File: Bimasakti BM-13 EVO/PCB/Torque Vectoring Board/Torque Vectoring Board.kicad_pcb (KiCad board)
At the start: 2 copper layers, 108 x 104.9 mm, 32 parts, among them J1 SIGNAL 1, J2 SIGNAL 2, U3 SN65HVD230, U4 SN65HVD230, U5 ADS1115IDGS

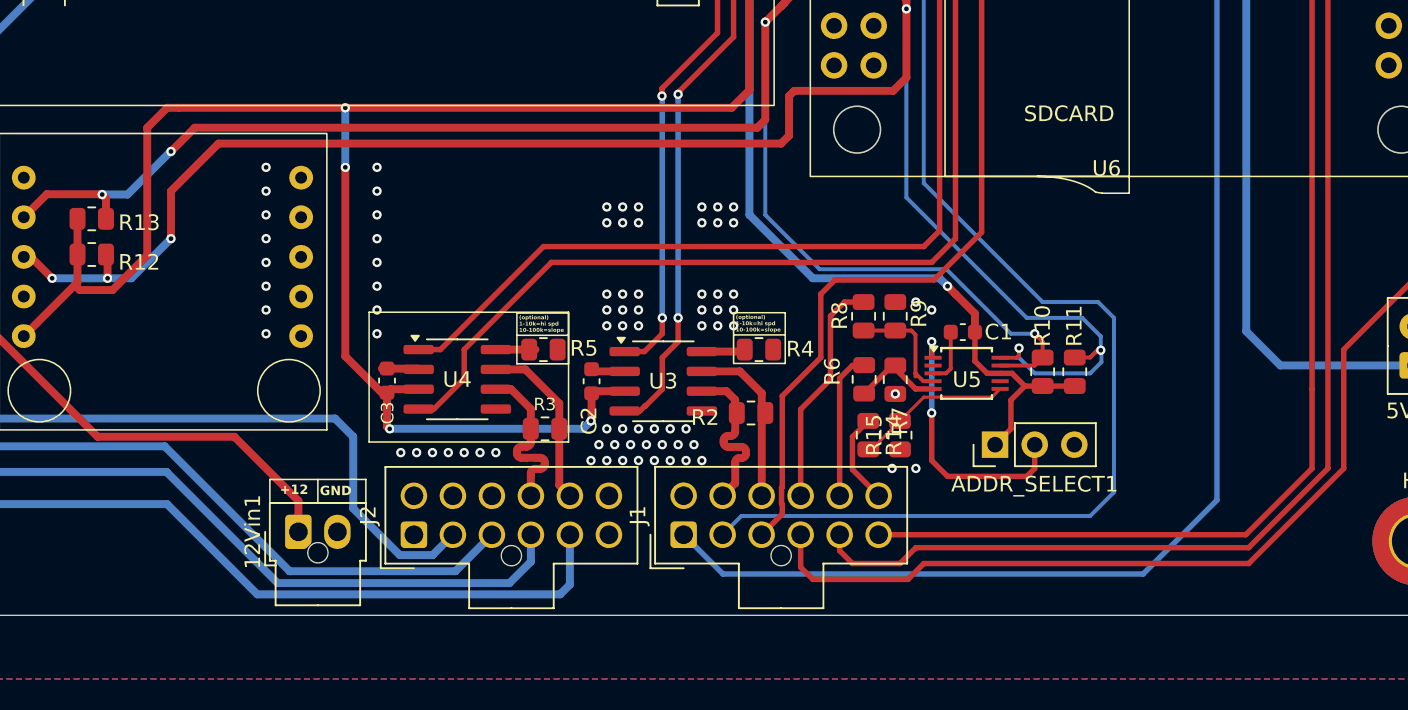
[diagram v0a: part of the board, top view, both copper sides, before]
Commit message: update footprint and pneumatic
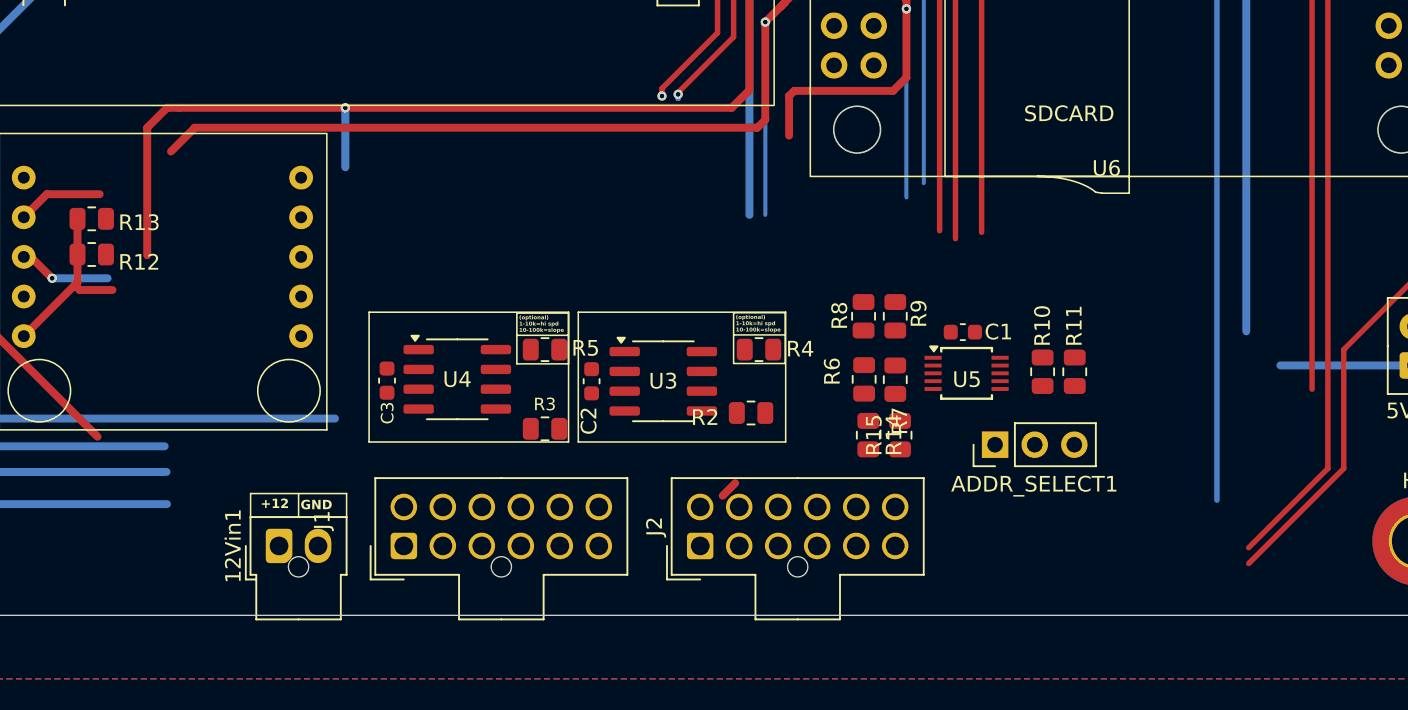
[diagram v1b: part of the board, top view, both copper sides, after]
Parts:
- moved J2 18.4 mm to (102.0, 134.0)
- moved J1 18.0 mm to (83.0, 134.0)
- moved 12Vin1 1.53 mm to (75.0, 134.0)
- moved R5 0.10 mm to (92.1, 121.4)
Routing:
- net SCL: track 115.5 -> 36.1 mm, vias 6 -> 2
- net 3V3: track 234.0 -> 161.6 mm, vias 7 -> 3
- net MISO: track 122.4 -> 69.3 mm
- net CAN2_RX: track 118.3 -> 78.3 mm
- net SCK: track 169.4 -> 132.2 mm
- net CAN2_TX: track 117.0 -> 80.5 mm
- net STM_RX: track 71.5 -> 36.8 mm
- net SDA: track 101.3 -> 68.5 mm, vias 4 -> 1
- net WS_FR: track 93.6 -> 61.9 mm
- net SS: track 165.7 -> 134.1 mm
- net MOSI: track 113.2 -> 84.2 mm
- net WS_FL: track 83.8 -> 55.2 mm
- net STM_TX: track 78.1 -> 50.1 mm
- net WS_RR: track 74.5 -> 49.3 mm
- net CAN1_RX: track 62.1 -> 40.0 mm, vias 2 -> 1
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
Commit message: update tv board
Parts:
- added J3: wsout1, TerminalBlock_Phoenix:TerminalBlock_Phoenix_PT-1,5-2-5.0-H_1x02_P5.00mm_Horizontal, F.Cu at (110.8, 42.9)
- added J4: wsout2, TerminalBlock_Phoenix:TerminalBlock_Phoenix_PT-1,5-2-5.0-H_1x02_P5.00mm_Horizontal, F.Cu at (122.5, 42.9)
- moved U1 90.8 mm to (83.3, 115.8), turned to 180 degrees
- moved U2 62.7 mm to (129.1, 139.6)
- moved R12 62.3 mm to (125.1, 120.9), turned to 180 degrees
- moved R13 62.3 mm to (125.1, 118.6), turned to 180 degrees
- moved U6 43.2 mm to (123.4, 36.2)
- moved R4 39.7 mm to (66.9, 113.4), turned to -90 degrees
- moved R2 36.1 mm to (69.3, 121.6)
- moved U3 29.1 mm to (71.7, 115.2), turned to 180 degrees
- moved ADDR_SELECT1 26.2 mm to (102.4, 109.0)
- moved R9 24.2 mm to (90.5, 122.7), turned to 0 degrees
- moved R8 22.6 mm to (90.5, 124.8), turned to 0 degrees
- moved C2 20.0 mm to (76.8, 115.3), turned to -90 degrees
- moved R3 19.7 mm to (109.0, 116.5), turned to -90 degrees
- moved C3 19.3 mm to (99.3, 115.0)
- moved R7 19.2 mm to (95.4, 122.7), turned to 0 degrees
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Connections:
- U1 pad 72: GPOS -> unconnected-(U1-PA6-Pad72)
- U6 pad 25: GND -> STM_RX
- U6 pad 26: GND -> unconnected-(U6-GND-Pad26)
- U6 pad 27: GND -> STM_TX
- U6 pad 29: GND -> SCL
- U6 pad 31: GND -> SDA
- U6 pad 4: GND -> WS_FRo
- U6 pad 5: GND -> WS_FLo
- U6 pad 6: GND -> WS_RRo
- U6 pad 7: GND -> WS_RLo
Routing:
- net STM_TX: track 50.1 -> 271.9 mm
- net STM_RX: track 36.8 -> 186.6 mm
- net SCL: track 36.1 -> 178.7 mm, vias 2 -> 0
- net SDA: track 68.5 -> 168.4 mm
- net SCK: track 132.2 -> 208.9 mm, vias 2 -> 0
- net SS: track 134.1 -> 204.4 mm
- net MISO: track 69.3 -> 137.9 mm
- net MOSI: track 84.2 -> 133.7 mm, vias 3 -> 0
- net 12V: track 79.1 -> 123.3 mm, vias 1 -> 0
- net WS_RLo: track 0.00 -> 43.0 mm
- net 3V3: track 161.6 -> 126.6 mm, vias 3 -> 1
- net 5V: track 156.8 -> 191.4 mm, vias 2 -> 1
- net ESC1_LO: track 0.00 -> 31.6 mm
- net WS_RRo: track 0.00 -> 31.4 mm
- net ESC1_HI: track 0.00 -> 30.7 mm
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
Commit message: tv dengan pdm kecil
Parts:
- added G***: LOGO, 0_logo:altium 12x12, F.Cu at (50.5, 117.5)
- added G***: LOGO, 0_logo:logo bimsak, F.Cu at (126.0, 111.0)
- added G***: LOGO, 0_logo:ugm 7.8x7.8, F.Cu at (134.5, 111.0)
- added a: LOGO, 0_logo:11jembo_tulisan_12x8.7, F.Cu at (51.0, 124.5)
- J3, J4: footprint TerminalBlock_Phoenix:TerminalBlock_Phoenix_PT-1,5-2-5.0-H_1x02_P5.00mm_Horizontal -> Connector_Molex:Molex_Nano-Fit_105309-xx02_1x02_P2.50mm_Vertical
- U6: footprint 0_CUSTOM_PCB:wheelspeed -> 0_WHEELSPEED:Untitled
- moved U6 25.6 mm to (114.3, 60.0)
- moved H4 10.2 mm to (138.0, 136.0)
- moved 5Vin1 9.99 mm to (138.3, 119.9)
- moved H2 9.95 mm to (138.0, 38.0)
- moved 12Vin1 9.88 mm to (65.3, 133.0)
- moved C1 9.88 mm to (102.1, 125.8)
- moved J1 9.88 mm to (73.3, 133.0)
- moved J2 9.88 mm to (92.3, 133.0)
- moved R10 9.88 mm to (103.8, 125.6)
- moved R12 9.88 mm to (115.4, 123.0)
- moved R13 9.88 mm to (115.4, 120.7)
- moved R4 9.88 mm to (57.2, 115.5)
- moved R5 9.88 mm to (99.8, 115.5)
- moved R8 9.88 mm to (80.9, 126.9)
- moved U5 9.88 mm to (97.9, 125.5)
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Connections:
- J1 pad 5: STM_TX -> STM_TX_2
- J1 pad 6: STM_RX -> STM_RX_2
- J2 pad 1: unconnected-(J2-Pin_1-Pad1) -> GND
- J2 pad 12: unconnected-(J2-Pin_12-Pad12) -> GND
- J2 pad 6: unconnected-(J2-Pin_6-Pad6) -> GND
- J2 pad 7: unconnected-(J2-Pin_7-Pad7) -> GND
- J2 pad 8: unconnected-(J2-Pin_8-Pad8) -> GND
- J2 pad 9: unconnected-(J2-Pin_9-Pad9) -> GND
- U1 pad 28: unconnected-(U1-PC12-Pad28) -> STM_TX_2
- U1 pad 29: unconnected-(U1-PD2-Pad29) -> STM_RX_2
- U6 pad 10: GND -> WS_RRo
- U6 pad 11: GND -> WS_FLo
- U6 pad 12: GND -> WS_FRo
- U6 pad 13: GND -> SDA
- U6 pad 14: GND -> SCL
- U6 pad 3: GND -> STM_TX
- U6 pad 4: WS_FRo -> STM_RX
- U6 pad 5: WS_FLo -> WS_RR
- U6 pad 6: WS_RRo -> WS_RL
- U6 pad 7: WS_RLo -> WS_FR
- U6 pad 8: GND -> WS_FL
- U6 pad 9: GND -> WS_RLo
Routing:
- net STM_TX: track 271.9 -> 110.9 mm, vias 0 -> 2
- net SCK: track 208.9 -> 91.7 mm
- net SS: track 204.4 -> 104.2 mm, vias 1 -> 0
- net STM_RX_2: track 0.00 -> 84.7 mm, vias 0 -> 1
- net STM_RX: track 186.6 -> 102.3 mm, vias 1 -> 2
- net 12V: track 123.3 -> 205.2 mm
- net SCL: track 178.7 -> 101.4 mm, vias 0 -> 1
- net STM_TX_2: track 0.00 -> 73.1 mm
- net SDA: track 168.4 -> 106.2 mm, vias 1 -> 0
- net WS_FRo: track 17.2 -> 65.0 mm
- net MOSI: track 133.7 -> 86.9 mm
- net MISO: track 137.9 -> 91.9 mm
- net WS_FLo: track 21.8 -> 58.6 mm
- net WS_RL: track 44.3 -> 78.8 mm
- net WS_RR: track 51.7 -> 77.8 mm, vias 0 -> 1
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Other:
- board size 108 x 104.9 mm -> 99 x 108 mm
- board text added: "5V"
- board text added: "APPS IN_1"
- board text added: "APPS IN_2"
- board text added: "ESC1 HI"
- board text added: "ESC1 LO"
- board text added: "ESC2 HI"
- board text added: "ESC2 LO"
- board text added: "MISO"
- board text added: "MOSI"
- board text added: "NC"
- board text added: "SCK"
- board text added: "SS"
- board text added: "STEER IN"
- board text added: "STM RX_2"
- board text added: "STM TX_2"
- board text added: "WS FL"
- board text added: "WS FR"
- board text added: "WS RL"
- board text added: "WS RR"
